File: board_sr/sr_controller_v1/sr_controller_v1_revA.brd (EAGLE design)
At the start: 140 x 150 mm, 122 parts, among them IC2 74HC595D, J2 WIRE_HOLE-14AWG, J3 WIRE_HOLE-14AWG, J4 WIRE_HOLE-14AWG, J5 WIRE_HOLE-14AWG, J6 WIRE_HOLE-14AWG, J7 WIRE_HOLE-14AWG, J8 WIRE_HOLE-14AWG, J9 WIRE_HOLE-14AWG, K1 G5L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

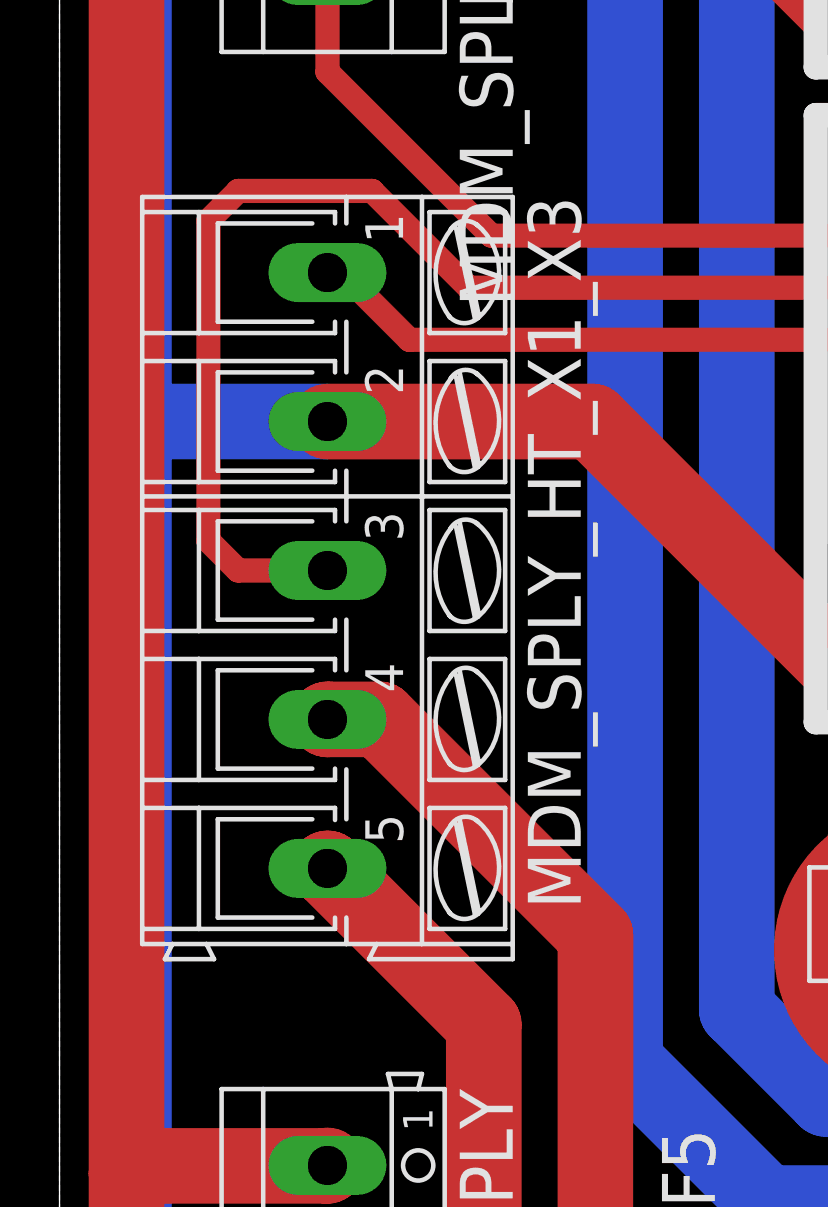
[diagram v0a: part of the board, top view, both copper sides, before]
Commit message: Add Casing CAD Drawing
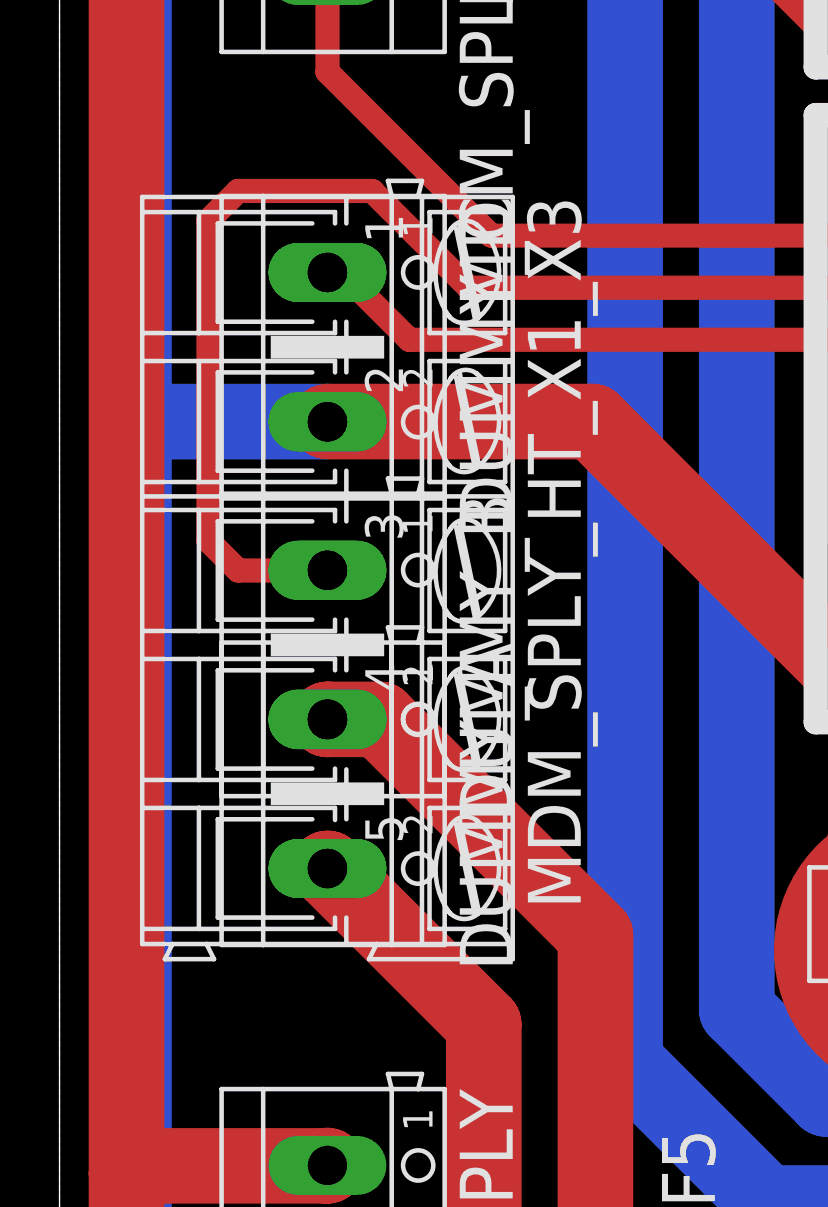
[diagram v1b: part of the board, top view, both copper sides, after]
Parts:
- added DUMMY_A, DUMMY_B, DUMMY_C: (no value), con-ptr500:AK500/2
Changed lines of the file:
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@@
 <element name="J8" library="powercube" package="WIRE_HOLE-14AWG" value="WIRE_HOLE-14AWG" x="28" y="9.5"/>
 <element name="J9" library="powercube" package="WIRE_HOLE-14AWG" value="WIRE_HOLE-14AWG" x="46" y="38.25"/>
+<element name="DUMMY_A" library="con-ptr500" package="AK500/2" value="" x="9" y="58" rot="R270">
+<attribute name="OC_NEWARK" value="unknown" x="9" y="58" size="1.778" layer="27" rot="R270" display="off"/>
+<attribute name="MPN" value="" x="9" y="58" size="1.778" layer="27" rot="R270" display="off"/>
+<attribute name="MF" value="" x="9" y="58" size="1.778" layer="27" rot="R270" display="off"/>
+<attribute name="OC_FARNELL" value="unknown" x="9" y="58" size="1.778" layer="27" rot="R270" display="off"/>
+</element>
+<element name="DUMMY_B" library="con-ptr500" package="AK500/2" value="" x="9" y="63" rot="R270">
+<attribute name="OC_NEWARK" value="unknown" x="9" y="63" size="1.778" layer="27" rot="R270" display="off"/>
+<attribute name="MPN" value="" x="9" y="63" size="1.778" layer="27" rot="R270" display="off"/>
+<attribute name="MF" value="" x="9" y="63" size="1.778" layer="27" rot="R270" display="off"/>
+<attribute name="OC_FARNELL" value="unknown" x="9" y="63" size="1.778" layer="27" rot="R270" display="off"/>
+</element>
+<element name="DUMMY_C" library="con-ptr500" package="AK500/2" value="" x="9" y="73" rot="R270">
+<attribute name="OC_NEWARK" value="unknown" x="9" y="73" size="1.778" layer="27" rot="R270" display="off"/>
+<attribute name="MPN" value="" x="9" y="73" size="1.778" layer="27" rot="R270" display="off"/>
+<attribute name="MF" value="" x="9" y="73" size="1.778" layer="27" rot="R270" display="off"/>
+<attribute name="OC_FARNELL" value="unknown" x="9" y="73" size="1.778" layer="27" rot="R270" display="off"/>
+</element>
 </elements>
 <signals>

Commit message: Initial commit of getSensorData
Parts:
- R11: value R2K -> R1K
- R15: value R2K -> R10K
- R17: value R5K -> R5.1K
- R29, R33: value R2K -> R5.1K
- R32: value R100K -> R270K
- R8: value R1K -> R220R
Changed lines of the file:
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@@
 <element name="R6" library="resistor" package="R0805" value="R1K" x="40.5" y="127.75" rot="MR0"/>
 <element name="R7" library="resistor" package="R0805" value="R10K" x="60.5" y="117" rot="MR270"/>
-<element name="R8" library="resistor" package="R0805" value="R1K" x="62.5" y="117" rot="MR90"/>
+<element name="R8" library="resistor" package="R0805" value="R220R" x="62.5" y="117" rot="MR90"/>
 <element name="U$2" library="SparkFun-AnalogIC" package="SO08" value="ACS712" x="59" y="107" rot="R270"/>
 <element name="C3" library="resistor" package="C0805K" value="C100N" x="65" y="109.25" rot="R180"/>
@@
 <element name="C6" library="resistor" package="C0805K" value="C1N" x="52.5" y="124" rot="MR270"/>
 <element name="R10" library="resistor" package="R0805" value="R10K" x="45" y="19.5"/>
-<element name="R11" library="resistor" package="R0805" value="R2K" x="45" y="17.5" rot="R180"/>
+<element name="R11" library="resistor" package="R0805" value="R1K" x="45" y="17.5" rot="R180"/>
 <element name="R12" library="resistor" package="R0805" value="R10K" x="45" y="9.5"/>
 <element name="R13" library="resistor" package="R0805" value="R1K" x="45" y="7.5" rot="R180"/>
 <element name="R14" library="resistor" package="R0805" value="R10K" x="122.5" y="18" rot="R90"/>
-<element name="R15" library="resistor" package="R0805" value="R2K" x="124.5" y="18" rot="R270"/>
+<element name="R15" library="resistor" package="R0805" value="R10K" x="124.5" y="18" rot="R270"/>
 <element name="R16" library="resistor" package="R0805" value="R10K" x="52.5" y="18" rot="R90"/>
-<element name="R17" library="resistor" package="R0805" value="R5K" x="54.5" y="18" rot="R270"/>
+<element name="R17" library="resistor" package="R0805" value="R5.1K" x="54.5" y="18" rot="R270"/>
 <element name="IC1" library="microbuilder" package="SIM900_SMT" value="" x="108" y="96.5" rot="R270"/>
 <element name="X1" library="microbuilder" package="SMA90_DIP" value="" x="135.5" y="98" rot="R270"/>
@@
 <element name="U$8" library="tigorcustom" package="SO16" value="74HC4053D" x="113.25" y="32.75"/>
 <element name="R28" library="resistor" package="R0805" value="R10K" x="112.5" y="18" rot="R90"/>
-<element name="R29" library="resistor" package="R0805" value="R2K" x="114.5" y="18" rot="R270"/>
+<element name="R29" library="resistor" package="R0805" value="R5.1K" x="114.5" y="18" rot="R270"/>
 <element name="R30" library="resistor" package="R0805" value="R1K" x="71.25" y="140.5" rot="R270"/>
 <element name="R31" library="resistor" package="R0805" value="R2K" x="71.25" y="136.5" rot="R270"/>
 <element name="U$9" library="bontor" package="TV16" value="TRANSFORMER" x="50" y="138"/>
-<element name="R32" library="resistor" package="0309/10" value="R100K" x="42.25" y="136.75" rot="MR270"/>
-<element name="R33" library="resistor" package="0309/10" value="R2K" x="57.5" y="138" rot="R90"/>
+<element name="R32" library="resistor" package="0309/10" value="R270K" x="42.25" y="136.75" rot="MR270"/>
+<element name="R33" library="resistor" package="0309/10" value="R5.1K" x="57.5" y="138" rot="R90"/>
 <element name="C14" library="resistor" package="C0805K" value="C100N" x="57.5" y="130" rot="MR90"/>
 <element name="R2" library="resistor" package="R0805" value="R10K" x="117.5" y="18" rot="R90"/>

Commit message: Update sensor code to del data from DB after read
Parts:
- F1, F5: value (none) -> 4A
- F3: value (none) -> 10A
- F4: value (none) -> 7A
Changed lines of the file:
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@@
 <attribute name="OC_FARNELL" value="unknown" x="65" y="10" size="1.778" layer="27" display="off"/>
 </element>
-<element name="F1" library="special" package="FUSE1" value="" x="61" y="46" rot="R90"/>
-<element name="F3" library="special" package="FUSE1" value="" x="51" y="46" rot="R90"/>
-<element name="F4" library="special" package="FUSE1" value="" x="41" y="46" rot="R90"/>
+<element name="F1" library="special" package="FUSE1" value="4A" x="61" y="46" rot="R90"/>
+<element name="F3" library="special" package="FUSE1" value="10A" x="51" y="46" rot="R90"/>
+<element name="F4" library="special" package="FUSE1" value="7A" x="41" y="46" rot="R90"/>
 <element name="INDICATOR_CONN" library="con-lstb" package="MA08-2" value="" x="117.5" y="136.75" rot="R90">
 <attribute name="OC_NEWARK" value="unknown" x="117.5" y="136.75" size="1.778" layer="27" rot="R90" display="off"/>
@@
 <attribute name="OC_FARNELL" value="unknown" x="119.5" y="10" size="1.778" layer="27" display="off"/>
 </element>
-<element name="F5" library="special" package="FUSE1" value="" x="29" y="46" rot="R90"/>
+<element name="F5" library="special" package="FUSE1" value="4A" x="29" y="46" rot="R90"/>
 <element name="MDM_SPLY_HT_X1_X3" library="con-ptr500" package="AK300/5" value="" x="9" y="65.5" rot="R270">
 <attribute name="OC_NEWARK" value="unknown" x="9" y="65.5" size="1.778" layer="27" rot="R270" display="off"/>

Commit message: Urgent Update board_sr only
Commited & Pussed by Maula
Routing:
- added copper zone on layer 16, net N$15
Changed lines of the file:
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@@
+</polygon>
+</signal>
+<signal name="N$15">
+<polygon width="0.4064" layer="16">
+<vertex x="-9" y="107"/>
+<vertex x="-4.5" y="107"/>
+<vertex x="-4.5" y="38"/>
+<vertex x="-9" y="38"/>
 </polygon>
 </signal>
